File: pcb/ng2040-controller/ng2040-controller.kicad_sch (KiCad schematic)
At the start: 21 parts, among them J1 A, J2 B, J3 C, J4 D, J5 START, J6 SELECT, J7 JOY, J8 BATTERY, J9 NRF24L01 Connector, SW1 OPTS, SW2 POWER, U1 RP2040-Zero, U3 MIC5205-3.0YM5

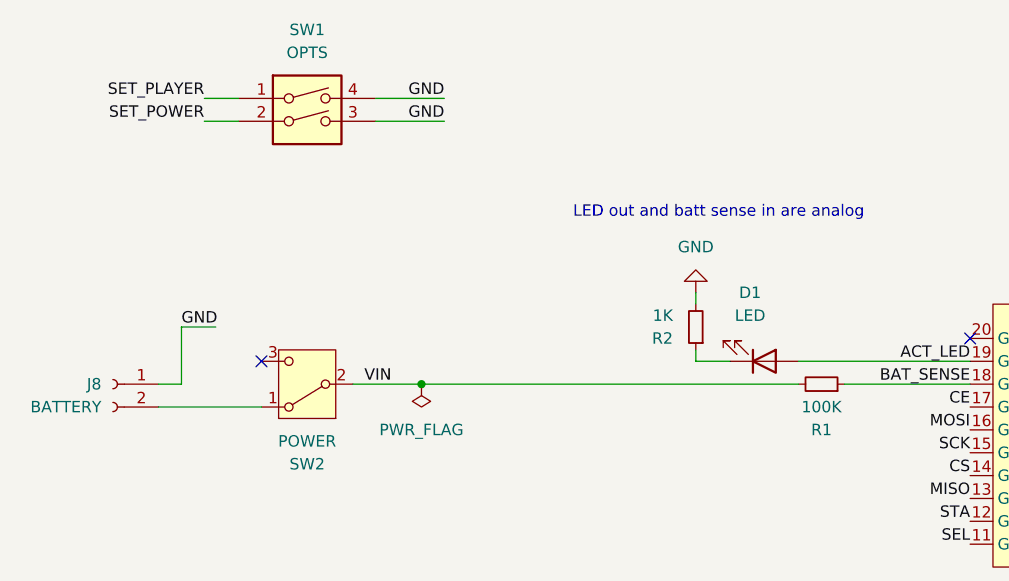
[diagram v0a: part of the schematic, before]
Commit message: Rerouting
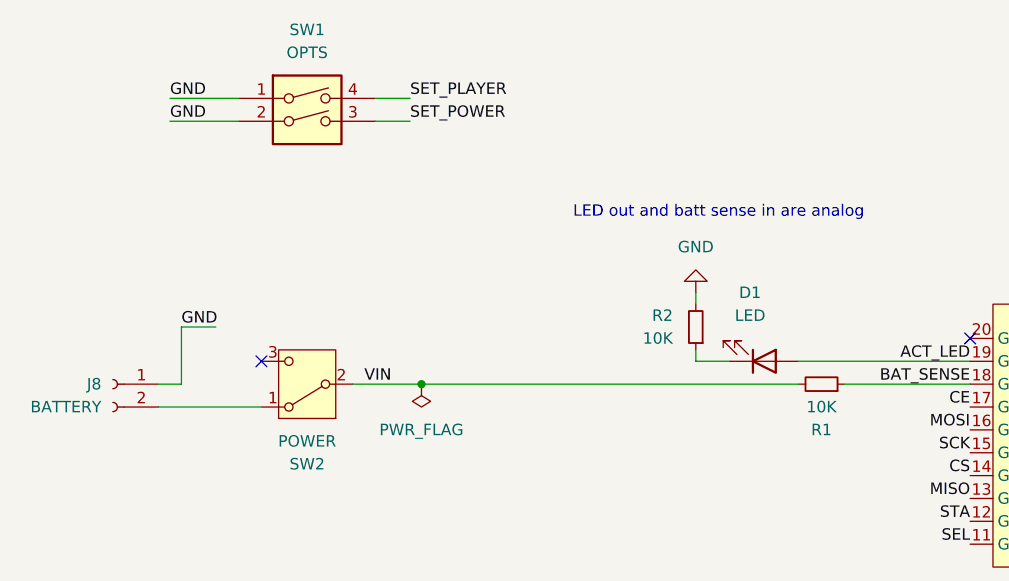
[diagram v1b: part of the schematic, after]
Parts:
- R1: value 100K -> 10K
- R2: value 1K -> 10K
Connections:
- net GND: now also SW1.1, SW1.2; no longer SW1.3, SW1.4
- net SET_PLAYER: now also SW1.4; no longer SW1.1
- net SET_POWER: now also SW1.3; no longer SW1.2
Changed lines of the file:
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@@
+	(wire
+		(pts
+			(xy 62.23 27.94) (xy 58.42 27.94)
+		)
+		(stroke
+			(width 0)
+			(type default)
+		)
+	)
 	(wire
 		(pts
@@
 	(wire
 		(pts
-			(xy 39.37 27.94) (xy 43.18 27.94)
-		)
-		(stroke
-			(width 0)
-			(type default)
-		)
-	)
-	(wire
-		(pts
-			(xy 58.42 30.48) (xy 66.04 30.48)
-		)
-		(stroke
-			(width 0)
-			(type default)
-		)
-	)
-	(wire
-		(pts
 			(xy 20.32 91.44) (xy 29.21 91.44)
 		)
@@
 	(wire
 		(pts
-			(xy 58.42 27.94) (xy 66.04 27.94)
-		)
-		(stroke
-			(width 0)
-			(type default)
-		)
-	)
-	(wire
-		(pts
-			(xy 39.37 30.48) (xy 43.18 30.48)
-		)
-		(stroke
-			(width 0)
-			(type default)
-		)
-	)
-	(wire
-		(pts
 			(xy 102.87 129.54) (xy 107.95 129.54)
 		)
@@
 	(wire
 		(pts
+			(xy 43.18 27.94) (xy 35.56 27.94)
+		)
+		(stroke
+			(width 0)
+			(type default)
+		)
+	)
+	(wire
+		(pts
 			(xy 93.98 50.8) (xy 93.98 49.53)
 		)
@@
 	(wire
 		(pts
+			(xy 62.23 30.48) (xy 58.42 30.48)
+		)
+		(stroke
+			(width 0)
+			(type default)
+		)
+	)
+	(wire
+		(pts
 			(xy 29.21 91.44) (xy 29.21 95.25)
 		)
@@
 		(pts
 			(xy 162.56 121.92) (xy 152.4 121.92)
+		)
+		(stroke
+			(width 0)
+			(type default)
+		)
+	)
+	(wire
+		(pts
+			(xy 43.18 30.48) (xy 35.56 30.48)
 		)
 		(stroke
@@
 	)
 	(label "GND"
-		(at 66.04 30.48 180)
-		(fields_autoplaced yes)
-		(effects
-			(font
-				(size 1.27 1.27)
-			)
-			(justify right bottom)
-		)
-	)
-	(label "GND"
 		(at 139.7 121.92 180)
 		(fields_autoplaced yes)
@@
 		)
 	)
-	(label "GND"
-		(at 66.04 27.94 180)
-		(fields_autoplaced yes)
-		(effects
-			(font
-				(size 1.27 1.27)
-			)
-			(justify right bottom)
-		)
-	)
 	(label "SEL"
 		(at 107.95 132.08 180)
@@
 		)
 	)
+	(label "SET_POWER"
+		(at 62.23 30.48 0)
+		(fields_autoplaced yes)
+		(effects
+			(font
+				(size 1.27 1.27)
+			)
+			(justify left bottom)
+		)
+	)
 	(label "CE"
 		(at 124.46 62.23 180)
@@
 		)
 	)
+	(label "SET_PLAYER"
+		(at 62.23 27.94 0)
+		(fields_autoplaced yes)
+		(effects
+			(font
+				(size 1.27 1.27)
+			)
+			(justify left bottom)
+		)
+	)
 	(label "DD"
 		(at 107.95 143.51 180)
@@
 		)
 	)
+	(label "GND"
+		(at 35.56 27.94 0)
+		(fields_autoplaced yes)
+		(effects
+			(font
+				(size 1.27 1.27)
+			)
+			(justify left bottom)
+		)
+	)
 	(label "STA"
 		(at 124.46 74.93 180)
@@
 		)
 	)
-	(label "SET_PLAYER"
-		(at 39.37 27.94 180)
-		(fields_autoplaced yes)
-		(effects
-			(font
-				(size 1.27 1.27)
-			)
-			(justify right bottom)
-		)
-	)
 	(label "CS"
 		(at 152.4 124.46 0)
@@
 		)
 	)
+	(label "GND"
+		(at 35.56 30.48 0)
+		(fields_autoplaced yes)
+		(effects
+			(font
+				(size 1.27 1.27)
+			)
+			(justify left bottom)
+		)
+	)
 	(label "MOSI"
 		(at 152.4 127 0)
@@
 			)
 			(justify left bottom)
-		)
-	)
-	(label "SET_POWER"
-		(at 39.37 30.48 180)
-		(fields_autoplaced yes)
-		(effects
-			(font
-				(size 1.27 1.27)
-			)
-			(justify right bottom)
 		)
 	)
@@
 			)
 		)
-		(property "Value" "100K"
+		(property "Value" "10K"
 			(at 107.95 62.23 90)
 			(effects
@@
 		(fields_autoplaced yes)
 		(property "Reference" "R2"
-			(at 91.44 54.6101 0)
+			(at 91.44 52.0699 0)
 			(effects
 				(font
@@
 			)
 		)
-		(property "Value" "1K"
-			(at 91.44 52.0701 0)
-			(effects
-				(font
+		(property "Value" "10K"
+			(at 91.44 54.6099 0)
+			(effects
+				(font

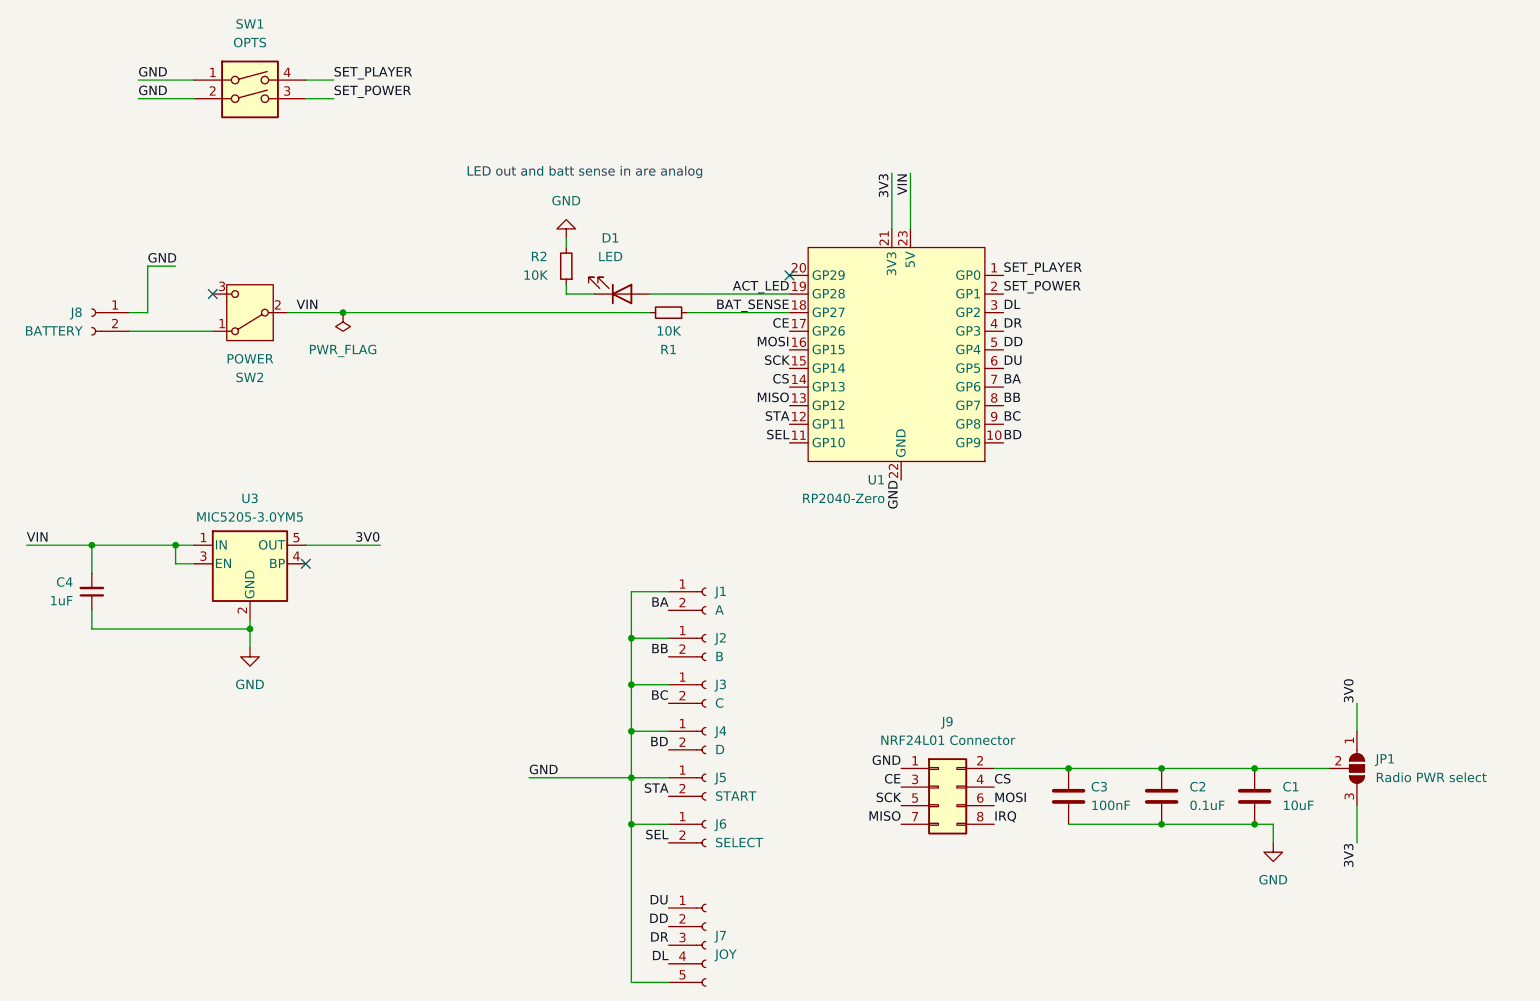
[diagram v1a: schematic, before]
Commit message: Committing to 3V reg, rewiring to use 3V reg to indirectly measure battery
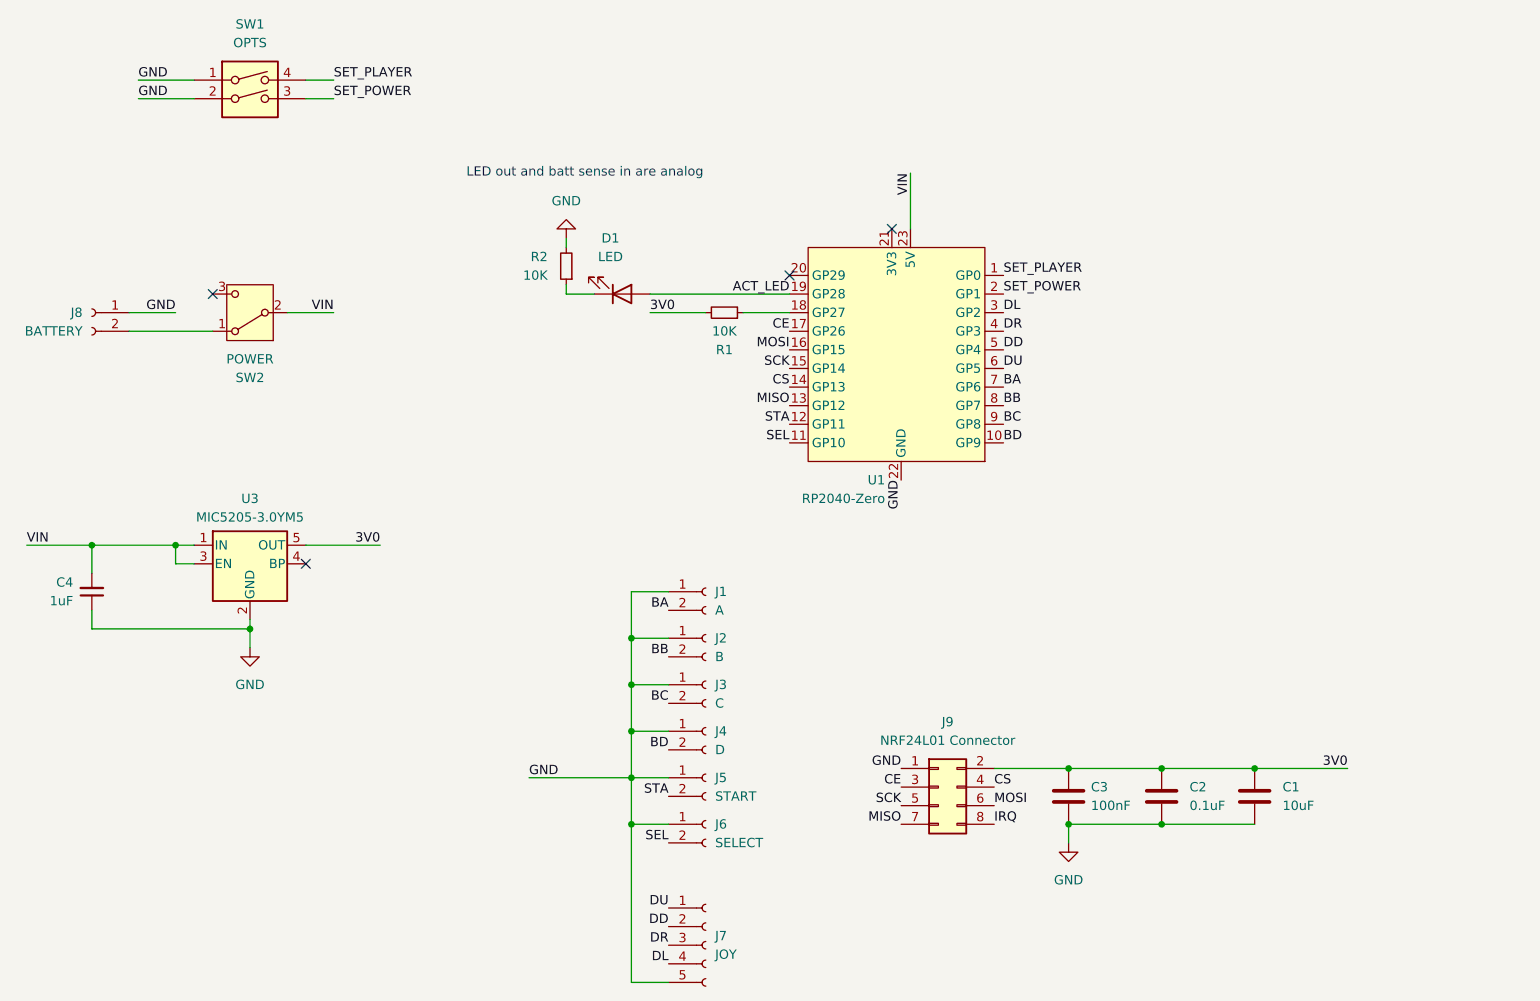
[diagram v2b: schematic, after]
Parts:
- removed JP1: Radio PWR select, Jumper:SolderJumper-3_P1.3mm_Open_RoundedPad1.0x1.5mm, symbol Jumper:SolderJumper_3_Open
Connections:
- net 3V0: now also C1.2, C2.2, C3.2, J9.2 (Pin_2), R1.2
- net VIN: no longer R1.2
- net 3V3: no longer names the net of U1.21 (3V3)
- net BAT_SENSE: no longer names the net of R1.1, U1.18 (GP27)
- no-connect marks 3 -> 4
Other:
- moved on the sheet: R1

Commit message: Minor noodling
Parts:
- U1: value RP2040-Zero -> RP2040 Tiny
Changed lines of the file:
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@@
 		(fields_autoplaced yes)
 		(property "Reference" "U1"
-			(at 137.5059 82.55 0)
+			(at 142.7165 82.55 0)
 			(effects
 				(font
 					(size 1.27 1.27)
 				)
-				(justify left)
+				(justify right)
 			)
 		)
-		(property "Value" "RP2040-Zero"
-			(at 137.5059 85.09 0)
+		(property "Value" "RP2040 Tiny"
+			(at 142.7165 85.09 0)
 			(effects
 				(font
 					(size 1.27 1.27)
 				)
-				(justify left)
+				(justify right)
 			)
 		)
